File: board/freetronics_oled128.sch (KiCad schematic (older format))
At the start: 42 parts, among them IC1 TPS61040, P1 CONN_10, P2 MICROSD, Q1 2N7002, Q2 2N7002

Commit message: Enlarge vias to standard size
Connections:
- wire segments 138 -> 167
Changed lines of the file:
@@
-EESchema Schematic File Version 2  date Wed 27 Feb 2013 11:41:00 EST
+EESchema Schematic File Version 2  date Thu 28 Feb 2013 10:01:17 EST
 LIBS:power
 LIBS:device
@@
 Sheet 1 1
 Title ""
-Date "22 feb 2013"
+Date "27 feb 2013"
 Rev ""
 Comp ""
@@
 $EndComp
 Wire Wire Line
-	1200 4500 900  4500
+	1200 4500 1050 4500
+Wire Wire Line
+	1050 4500 900  4500
 Connection ~ 5450 3050
 Wire Wire Line
-	6000 2200 6000 4200
+	6000 2200 6000 3850
+Wire Wire Line
+	6000 3850 6000 4200
 Wire Wire Line
 	750  2200 1250 2200
@@
 	10100 2500 9500 2500
 Wire Wire Line
-	10100 2750 10100 2400
+	10100 2750 10100 2600
+Wire Wire Line
+	10100 2600 10100 2500
+Wire Wire Line
+	10100 2500 10100 2400
 Wire Wire Line
 	10100 2400 9500 2400
@@
 	10450 2850 10450 2900
 Wire Wire Line
-	10800 3450 10800 1400
+	10800 3450 10800 3400
+Wire Wire Line
+	10800 3400 10800 1400
 Wire Wire Line
 	10800 1400 9500 1400
@@
 	2500 2900 2800 2900
 Wire Wire Line
-	4850 3050 5500 3050
+	4850 3050 5450 3050
+Wire Wire Line
+	5450 3050 5500 3050
 Wire Wire Line
 	5300 3850 4850 3850
@@
 	750  4750 900  4750
 Wire Wire Line
-	900  4900 900  4600
+	900  4900 900  4750
+Wire Wire Line
+	900  4750 900  4600
 Connection ~ 1050 4500
 Wire Wire Line
@@
 	4150 5800 4150 6050
 Wire Wire Line
-	3050 6500 4150 6500
-Wire Wire Line
-	5400 5800 3550 5800
+	3050 6500 3750 6500
+Wire Wire Line
+	3750 6500 4150 6500
+Wire Wire Line
+	5400 5800 4950 5800
+Wire Wire Line
+	4950 5800 4500 5800
+Wire Wire Line
+	4500 5800 4150 5800
+Wire Wire Line
+	4150 5800 3750 5800
+Wire Wire Line
+	3750 5800 3550 5800
 Connection ~ 4950 5800
 Connection ~ 4150 5800
@@
 Connection ~ 7450 2400
 Wire Wire Line
-	7800 2400 6700 2400
+	7800 2400 7450 2400
+Wire Wire Line
+	7450 2400 6700 2400
 Wire Wire Line
 	7100 3000 7100 3200
@@
 Connection ~ 5000 2200
 Wire Wire Line
-	5100 2200 4700 2200
+	5100 2200 5000 2200
+Wire Wire Line
+	5000 2200 4900 2200
+Wire Wire Line
+	4900 2200 4800 2200
+Wire Wire Line
+	4800 2200 4700 2200
 Wire Wire Line
 	4250 3500 4250 3600
@@
 	7450 3000 7450 3200
 Wire Wire Line
-	7800 2300 7800 2600
+	7800 2300 7800 2400
+Wire Wire Line
+	7800 2400 7800 2600
 Connection ~ 7800 2400
 Connection ~ 850  5800
 Wire Wire Line
-	3150 5800 2800 5800
+	3150 5800 3050 5800
+Wire Wire Line
+	3050 5800 2800 5800
 Wire Wire Line
 	3300 6350 3050 6350
@@
 Connection ~ 3750 6500
 Wire Wire Line
-	700  5800 2200 5800
+	700  5800 850  5800
+Wire Wire Line
+	850  5800 1400 5800
+Wire Wire Line
+	1400 5800 1900 5800
+Wire Wire Line
+	1900 5800 2200 5800
 Wire Wire Line
 	3750 5800 3750 6000
@@
 	1900 7050 1900 7100
 Wire Wire Line
-	1550 6500 1950 6500
+	1550 6500 1900 6500
+Wire Wire Line
+	1900 6500 1950 6500
 Connection ~ 1900 6500
 Wire Wire Line
@@
 	2550 1200 2550 1050
 Wire Wire Line
-	2500 1050 2950 1050
+	2500 1050 2550 1050
+Wire Wire Line
+	2550 1050 2950 1050
 Wire Wire Line
 	5400 2650 5400 2200
 Wire Wire Line
-	5800 3600 5800 3250
+	5800 3600 5800 3550
+Wire Wire Line
+	5800 3550 5800 3250
 Connection ~ 5800 3550
 Wire Wire Line
@@
 	5300 4100 4850 4100
 Wire Wire Line
-	5900 2850 5500 2850
+	5900 2850 5800 2850
+Wire Wire Line
+	5800 2850 5500 2850
 Connection ~ 5800 2850
 Wire Wire Line
-	6250 2550 6250 4200
+	6250 2550 6250 4100
+Wire Wire Line
+	6250 4100 6250 4200
 Wire Wire Line
 	9500 1700 9900 1700
@@
 Connection ~ 10800 4150
 Wire Wire Line
-	10800 4200 10800 3850
+	10800 4200 10800 4150
+Wire Wire Line
+	10800 4150 10800 3850
 Wire Wire Line
 	10450 4150 10800 4150
@@
 Connection ~ 10100 2600
 Wire Wire Line
-	9500 3650 10500 3650
+	9500 3650 10450 3650
+Wire Wire Line
+	10450 3650 10500 3650
 Wire Wire Line
 	750  1500 1250 1500
@@
 Connection ~ 10450 3650
 Wire Wire Line
-	900  4500 900  4150
+	900  4500 900  4350
+Wire Wire Line
+	900  4350 900  4150
 $Comp
 L PWR_FLAG #FLG02

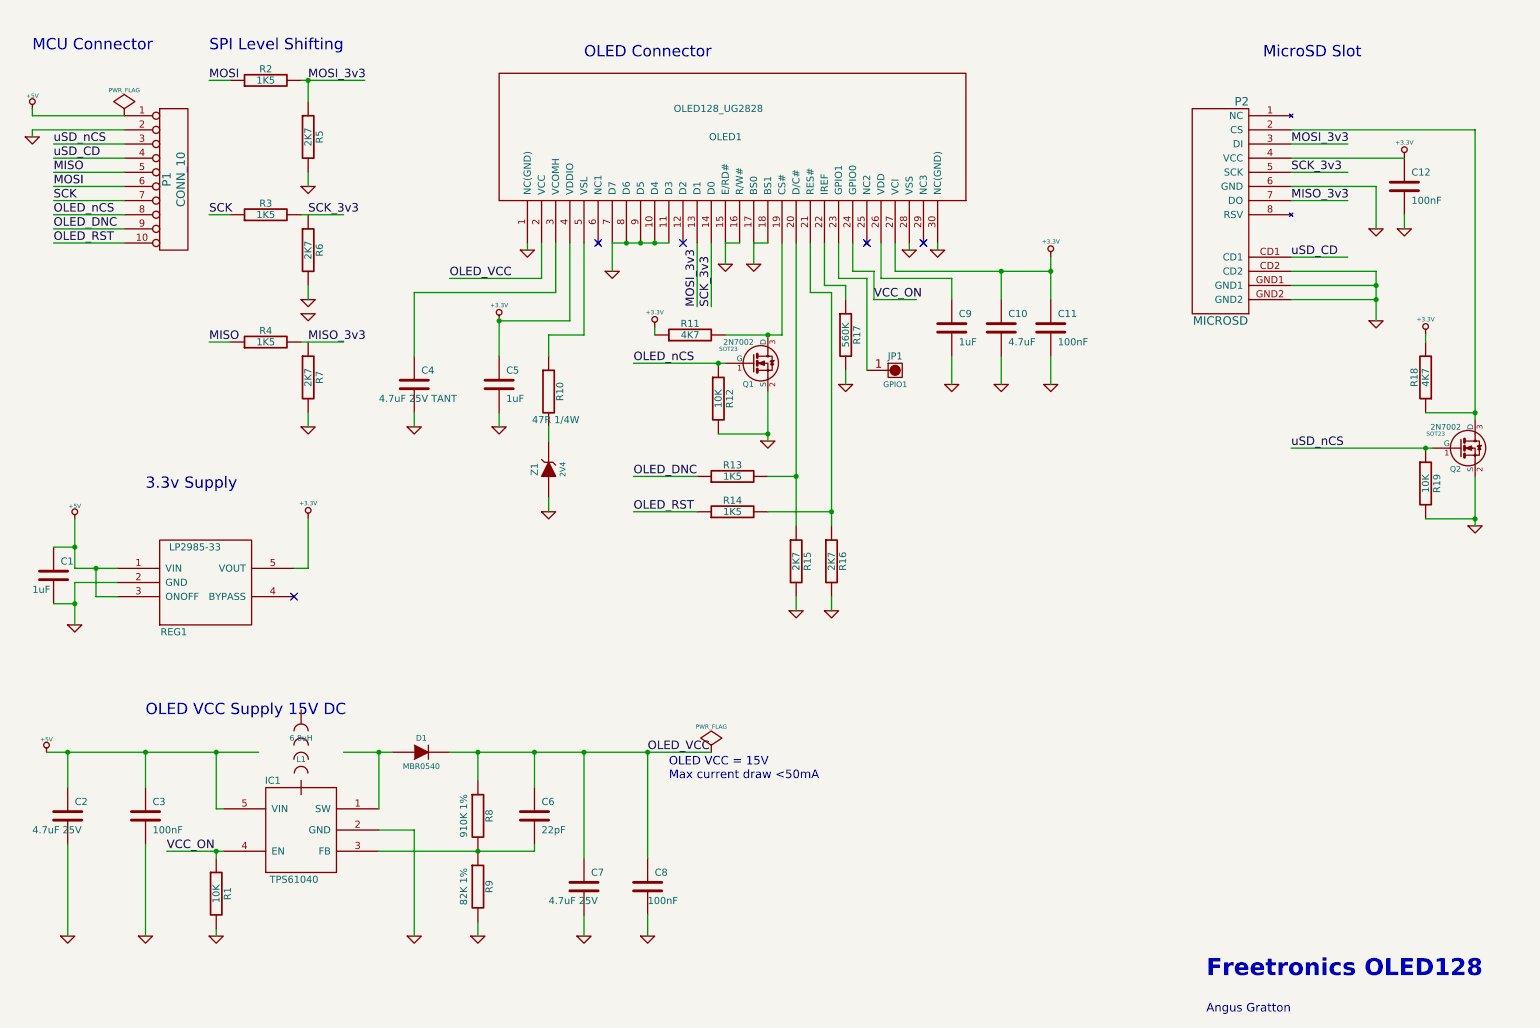
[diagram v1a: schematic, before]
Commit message: Refactor schematic to flow-to-right
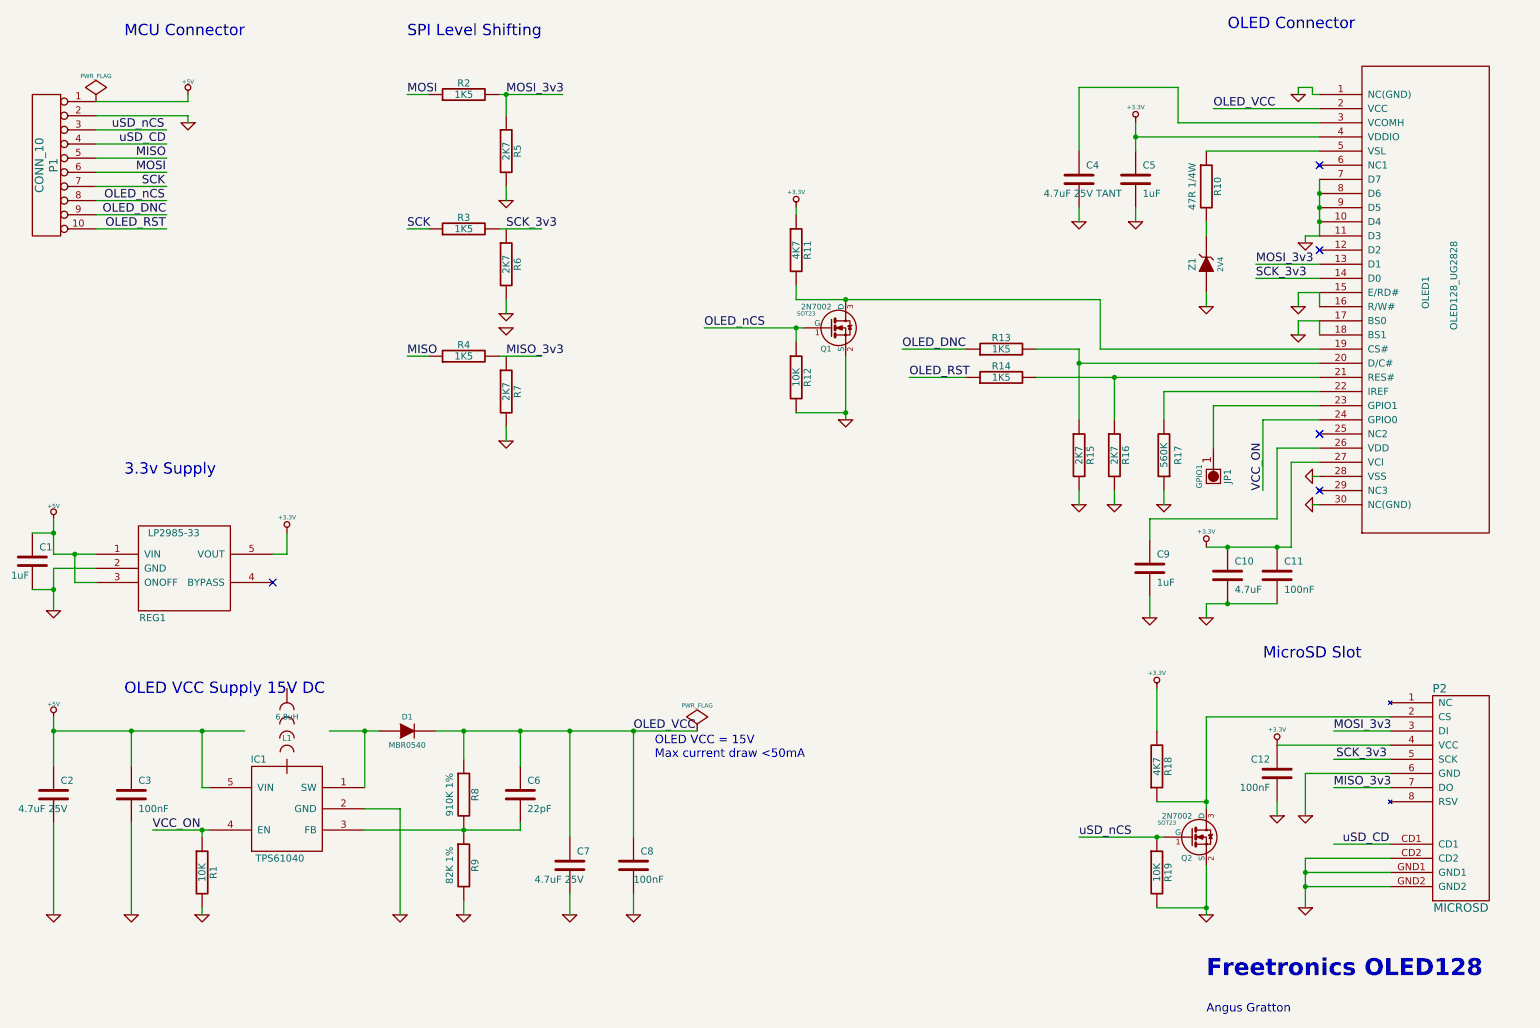
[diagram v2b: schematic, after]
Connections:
- wire segments 167 -> 170
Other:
- moved on the sheet: C1, C10, C11, C12, C2, C3, C4, C5, C6, C7, C8, C9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

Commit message: Add silkscreen content, logos
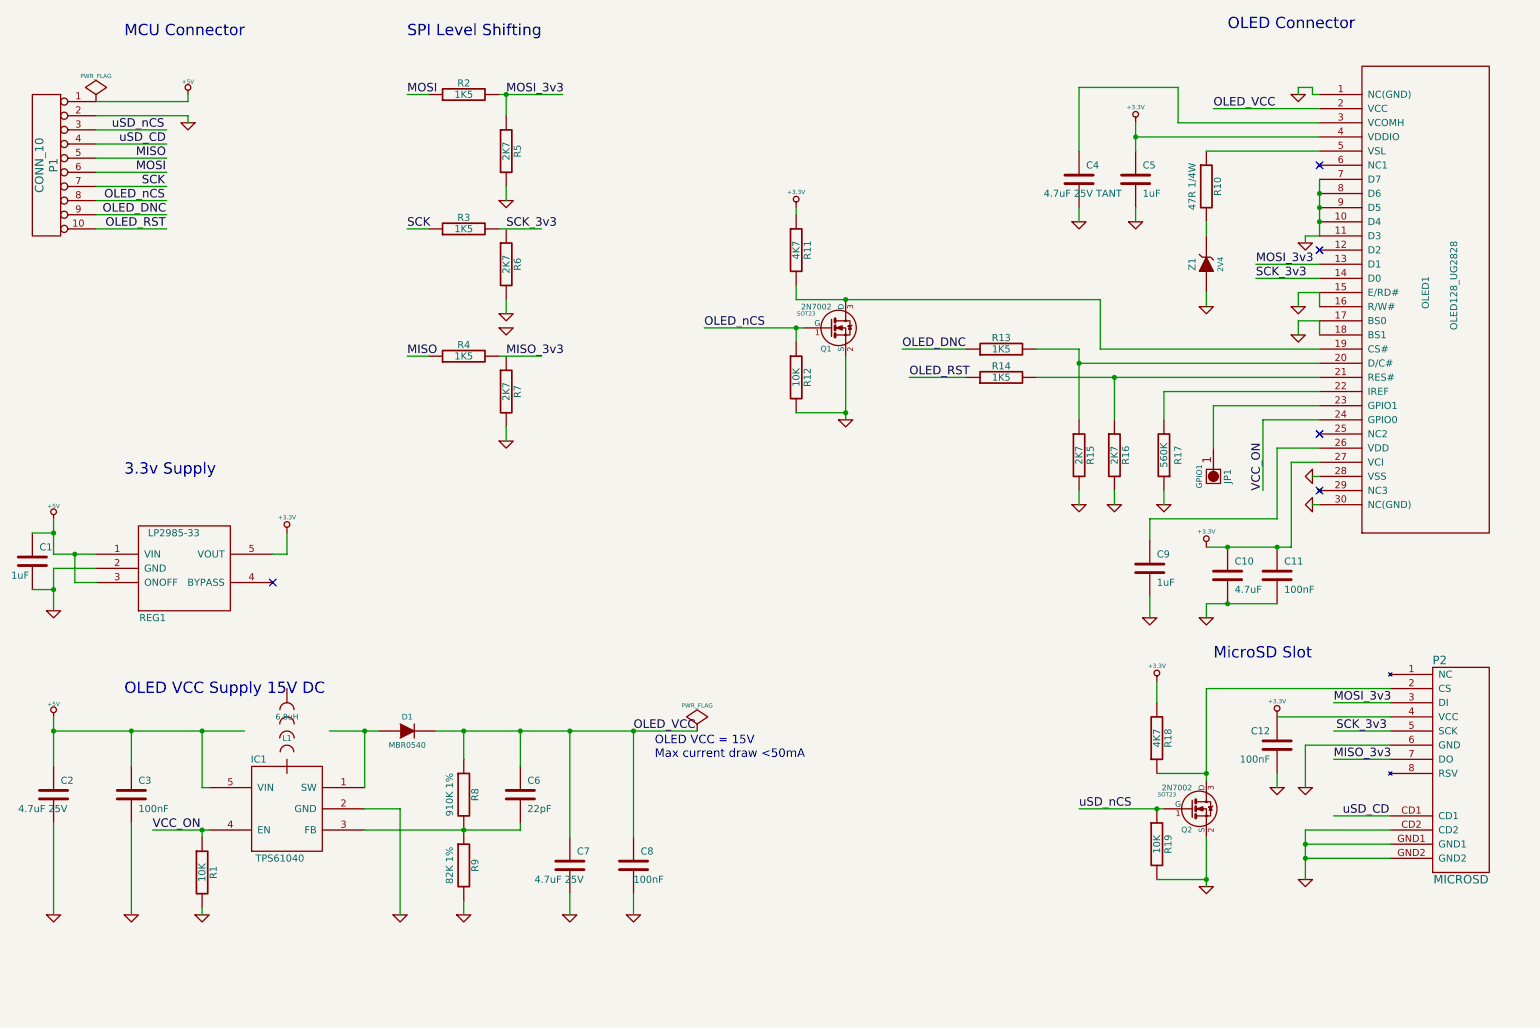
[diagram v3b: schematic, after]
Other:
- note removed: "Angus Gratton"
- note removed: "Freetronics OLED128"
- moved on the sheet: C12, P2, Q2, R18, R19
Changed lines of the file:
@@
-EESchema Schematic File Version 2  date Thu 28 Feb 2013 12:13:40 EST
+EESchema Schematic File Version 2  date Thu 28 Feb 2013 12:36:34 EST
 LIBS:power
 LIBS:device
@@
 encoding utf-8
 Sheet 1 1
-Title ""
+Title "Freetronics OLED128              http://www.freetronics.com/oled128"
 Date "28 feb 2013"
-Rev ""
-Comp ""
-Comment1 ""
-Comment2 ""
+Rev "0.9"
+Comp "(C)2013 Freetronics Pty Ltd"
+Comment1 "Released under TAPR Open Hardware License www.tapr.org/ohl"
+Comment2 "SKU: OLED128"
 Comment3 ""
 Comment4 ""
@@
 	9400 4150 8500 4150
 Wire Wire Line
-	8900 4850 8900 4750
+	8900 4750 8900 4850
 Connection ~ 9400 4350
 Wire Wire Line
 	8500 4700 8500 4850
 Wire Wire Line
-	8900 6200 8900 6150
-Wire Wire Line
-	8900 6150 8900 5550
-Wire Wire Line
-	750  4150 750  4250
-Wire Wire Line
-	750  4250 750  4400
-Connection ~ 8550 6400
+	8900 6000 8900 5950
+Wire Wire Line
+	8900 5950 8900 5350
+Wire Wire Line
+	750  4400 750  4250
+Wire Wire Line
+	750  4250 750  4150
+Connection ~ 8550 6200
 Wire Wire Line
 	1550 1400 1050 1400
 Wire Wire Line
-	8600 6400 8550 6400
-Wire Wire Line
-	8550 6400 8000 6400
-Connection ~ 9600 6750
-Wire Wire Line
-	9600 6750 10200 6750
-Wire Wire Line
-	9800 6450 10200 6450
-Wire Wire Line
-	8550 6900 8900 6900
-Wire Wire Line
-	8900 6600 8900 6900
-Wire Wire Line
-	8900 6900 8900 6950
-Connection ~ 8900 6900
-Wire Wire Line
-	9400 6150 9400 6250
-Wire Wire Line
-	9600 6250 9600 5950
-Wire Wire Line
-	9600 5950 10200 5950
-Wire Wire Line
-	10200 5850 9800 5850
+	8600 6200 8550 6200
+Wire Wire Line
+	8550 6200 8000 6200
+Connection ~ 9600 6550
+Wire Wire Line
+	9600 6550 10200 6550
+Wire Wire Line
+	9800 6250 10200 6250
+Wire Wire Line
+	8550 6700 8900 6700
+Wire Wire Line
+	8900 6400 8900 6700
+Wire Wire Line
+	8900 6700 8900 6750
+Connection ~ 8900 6700
+Wire Wire Line
+	9400 5950 9400 6050
+Wire Wire Line
+	9600 6050 9600 5750
+Wire Wire Line
+	9600 5750 10200 5750
+Wire Wire Line
+	10200 5650 9800 5650
 Wire Wire Line
 	9250 2450 9700 2450
@@
 	600  4250 750  4250
 Wire Wire Line
-	1050 4500 750  4500
+	750  4500 1050 4500
 Connection ~ 1800 6350
 Wire Wire Line
@@
 	1800 6900 1800 6950
 Wire Wire Line
-	750  5650 750  5900
+	750  5900 750  5650
+Wire Wire Line
+	750  5650 750  5550
 Wire Wire Line
 	1300 6300 1300 6950
@@
 Wire Wire Line
 	1300 5650 750  5650
-Wire Wire Line
-	750  5650 750  5550
 Connection ~ 3650 6350
 Wire Wire Line
-	4050 6300 4050 6350
+	4050 6350 4050 6300
 Connection ~ 4400 5650
 Wire Wire Line
@@
 	4850 5650 5300 5650
 Wire Wire Line
-	4050 6350 3650 6350
-Wire Wire Line
-	3650 6350 2950 6350
+	2950 6350 3650 6350
+Wire Wire Line
+	3650 6350 4050 6350
 Wire Wire Line
 	4050 5650 4050 5900
@@
 	1800 6400 1800 6350
 Wire Wire Line
-	900  4400 900  4600
+	900  4600 900  4400
 Wire Wire Line
 	900  4600 1050 4600
 Connection ~ 900  4400
 Wire Wire Line
-	750  4500 750  4650
-Wire Wire Line
-	750  4650 750  4800
+	750  4800 750  4650
+Wire Wire Line
+	750  4650 750  4500
 Wire Wire Line
 	600  4650 750  4650
@@
 	3950 3600 3950 3500
 Wire Wire Line
-	9800 5650 10200 5650
-Wire Wire Line
-	10200 6050 9800 6050
-Wire Wire Line
-	10200 5750 9400 5750
-Wire Wire Line
-	8900 5550 10200 5550
-Wire Wire Line
-	10200 6550 9600 6550
-Wire Wire Line
-	9600 6550 9600 6650
-Wire Wire Line
-	9600 6650 9600 6750
-Wire Wire Line
-	9600 6750 9600 6900
-Wire Wire Line
-	9600 6650 10200 6650
-Connection ~ 9600 6650
-Wire Wire Line
-	8550 6150 8900 6150
-Connection ~ 8900 6150
+	9800 5450 10200 5450
+Wire Wire Line
+	10200 5850 9800 5850
+Wire Wire Line
+	10200 5550 9400 5550
+Wire Wire Line
+	8900 5350 10200 5350
+Wire Wire Line
+	9600 6350 10200 6350
+Wire Wire Line
+	9600 6700 9600 6550
+Wire Wire Line
+	9600 6550 9600 6450
+Wire Wire Line
+	9600 6450 9600 6350
+Wire Wire Line
+	9600 6450 10200 6450
+Connection ~ 9600 6450
+Wire Wire Line
+	8550 5950 8900 5950
+Connection ~ 8900 5950
 Wire Wire Line
 	1550 1500 1050 1500
@@
 	1550 2100 1050 2100
 Wire Wire Line
-	750  4400 900  4400
-Wire Wire Line
-	900  4400 1050 4400
-Wire Wire Line
-	8550 5350 8550 5650
-Wire Wire Line
-	9500 3750 9500 4350
-Wire Wire Line
-	9500 4350 9400 4350
-Wire Wire Line
-	9400 4350 9050 4350
-Wire Wire Line
-	9050 4350 8900 4350
+	1050 4400 900  4400
+Wire Wire Line
+	900  4400 750  4400
+Wire Wire Line
+	8550 5300 8550 5450
+Wire Wire Line
+	9500 4350 9500 3750
+Wire Wire Line
+	8900 4350 9050 4350
+Wire Wire Line
+	9050 4350 9400 4350
+Wire Wire Line
+	9400 4350 9500 4350
 Connection ~ 9050 4350
 Wire Wire Line
-	8900 4750 9050 4750
-Wire Wire Line
-	9050 4750 9400 4750
+	9400 4750 9050 4750
+Wire Wire Line
+	9050 4750 8900 4750
 Connection ~ 9050 4750
 Wire Wire Line
@@
 	9700 3050 8000 3050
 Wire Wire Line
-	7700 2950 8000 2950
-Wire Wire Line
-	8000 2950 8000 3050
-Wire Wire Line
-	8000 3050 8000 3450
+	8000 2950 7700 2950
+Wire Wire Line
+	8000 3450 8000 3050
+Wire Wire Line
+	8000 3050 8000 2950
 Connection ~ 6350 3400
 Wire Wire Line
@@
 L MICROSD P2
 U 1 1 51259AC5
-P 10650 6250
-F 0 "P2" H 10750 7150 60  0000 C CNN
-F 1 "MICROSD" H 10600 5600 60  0000 C CNN
-	1    10650 6250
+P 10650 6050
+F 0 "P2" H 10750 6950 60  0000 C CNN
+F 1 "MICROSD" H 10600 5400 60  0000 C CNN
+	1    10650 6050
 	-1   0    0    -1
 $EndComp
@@
 Text Label 1332 1600 0    60   ~ 0
 MISO
-Text Notes 9300 5150 0    80   ~ 0
+Text Notes 8950 5150 0    80   ~ 0
 MicroSD Slot
 $Comp
 L GND #PWR04
 U 1 1 51243989
-P 9600 6900
-F 0 "#PWR04" H 9600 6900 30  0001 C CNN
-F 1 "GND" H 9600 6830 30  0001 C CNN
-	1    9600 6900
-	-1   0    0    -1
-$EndComp
-Text Label 9864 6450 0    60   ~ 0
+P 9600 6700
+F 0 "#PWR04" H 9600 6700 30  0001 C CNN
+F 1 "GND" H 9600 6630 30  0001 C CNN
+	1    9600 6700
+	-1   0    0    -1
+$EndComp
+Text Label 9864 6250 0    60   ~ 0
 uSD_CD
 $Comp
 L +3.3V #PWR05
 U 1 1 512438D6
-P 8550 5350
-F 0 "#PWR05" H 8550 5310 30  0001 C CNN
-F 1 "+3.3V" H 8550 5460 30  0000 C CNN
-	1    8550 5350
+P 8550 5300
+F 0 "#PWR05" H 8550 5260 30  0001 C CNN
+F 1 "+3.3V" H 8550 5410 30  0000 C CNN
+	1    8550 5300
 	-1   0    0    -1
 $EndComp
@@
 L R R18
 U 1 1 512438D5
-P 8550 5900
-F 0 "R18" V 8630 5900 50  0000 C CNN
-F 1 "4K7" V 8550 5900 50  0000 C CNN
-	1    8550 5900
+P 8550 5700
+F 0 "R18" V 8630 5700 50  0000 C CNN
+F 1 "4K7" V 8550 5700 50  0000 C CNN
+	1    8550 5700
 	1    0    0    1
 $EndComp
-Text Label 8000 6400 0    60   ~ 0
+Text Label 8000 6200 0    60   ~ 0
 uSD_nCS
 $Comp
 L 2N7002 Q2
 U 1 1 512438C2
-P 8800 6400
-F 0 "Q2" H 8800 6252 40  0000 R CNN
-F 1 "2N7002" H 8800 6549 40  0000 R CNN
-F 2 "SOT23" H 8621 6501 29  0000 C CNN
-	1    8800 6400
+P 8800 6200
+F 0 "Q2" H 8800 6052 40  0000 R CNN
+F 1 "2N7002" H 8800 6349 40  0000 R CNN
+F 2 "SOT23" H 8621 6301 29  0000 C CNN
+	1    8800 6200
 	1    0    0    -1
 $EndComp
@@
 L R R19
 U 1 1 512438C1
-P 8550 6650
-F 0 "R19" V 8630 6650 50  0000 C CNN
-F 1 "10K" V 8550 6650 50  0000 C CNN
-	1    8550 6650
+P 8550 6450
+F 0 "R19" V 8630 6450 50  0000 C CNN
+F 1 "10K" V 8550 6450 50  0000 C CNN
+	1    8550 6450
 	1    0    0    -1
 $EndComp
@@
 L GND #PWR06
 U 1 1 512438C0
-P 8900 6950
-F 0 "#PWR06" H 8900 6950 30  0001 C CNN
-F 1 "GND" H 8900 6880 30  0001 C CNN
-	1    8900 6950
+P 8900 6750
+F 0 "#PWR06" H 8900 6750 30  0001 C CNN
+F 1 "GND" H 8900 6680 30  0001 C CNN
+	1    8900 6750
 	1    0    0    -1
 $EndComp
@@
 L GND #PWR07
 U 1 1 51243728
-P 9400 6250
-F 0 "#PWR07" H 9400 6250 30  0001 C CNN
-F 1 "GND" H 9400 6180 30  0001 C CNN
-	1    9400 6250
+P 9400 6050
+F 0 "#PWR07" H 9400 6050 30  0001 C CNN
+F 1 "GND" H 9400 5980 30  0001 C CNN
+	1    9400 6050
 	-1   0    0    -1
 $EndComp
@@
 L C C12
 U 1 1 512436E0
-P 9400 5950
-F 0 "C12" H 9450 6050 50  0000 L CNN
-F 1 "100nF" H 9450 5850 50  0000 L CNN
-	1    9400 5950
+P 9400 5750
+F 0 "C12" H 9450 5850 50  0000 L CNN
+F 1 "100nF" H 9450 5650 50  0000 L CNN
+	1    9400 5750
 	-1   0    0    -1
 $EndComp
@@
 L +3.3V #PWR08
 U 1 1 512436A9
-P 9400 5750
-F 0 "#PWR08" H 9400 5710 30  0001 C CNN
-F 1 "+3.3V" H 9400 5860 30  0000 C CNN
-	1    9400 5750
+P 9400 5550
+F 0 "#PWR08" H 9400 5510 30  0001 C CNN
+F 1 "+3.3V" H 9400 5660 30  0000 C CNN
+	1    9400 5550
 	-1   0    0    -1
 $EndComp
@@
 L GND #PWR09
 U 1 1 51243692
-P 9600 6250
-F 0 "#PWR09" H 9600 6250 30  0001 C CNN
-F 1 "GND" H 9600 6180 30  0001 C CNN
-	1    9600 6250
-	-1   0    0    -1
-$EndComp
-Text Label 9800 6050 0    60   ~ 0
+P 9600 6050
+F 0 "#PWR09" H 9600 6050 30  0001 C CNN
+F 1 "GND" H 9600 5980 30  0001 C CNN
+	1    9600 6050
+	-1   0    0    -1
+$EndComp
+Text Label 9800 5850 0    60   ~ 0
 MISO_3v3
-Text Label 9818 5850 0    60   ~ 0
+Text Label 9818 5650 0    60   ~ 0
 SCK_3v3
-Text Label 9800 5650 0    60   ~ 0
+Text Label 9800 5450 0    60   ~ 0
 MOSI_3v3
 Text Notes 3250 750  0    80   ~ 0
@@
 Text Notes 9050 700  0    80   ~ 0
 OLED Connector
-Text Notes 8900 7650 0    60   ~ 0
-Angus Gratton
-Text Notes 8900 7400 0    120  ~ 24
-Freetronics OLED128
 Text Notes 1250 5400 0    80   ~ 0
 OLED VCC Supply 15V DC
